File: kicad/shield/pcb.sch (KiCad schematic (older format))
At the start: 10 parts, among them J1 Conn_01x12_Fem_l, J2 Conn_01x12_Fem_r, J3 Conn_01x12_Fem_b_r, J4 Conn_01x09_Fem_b_l

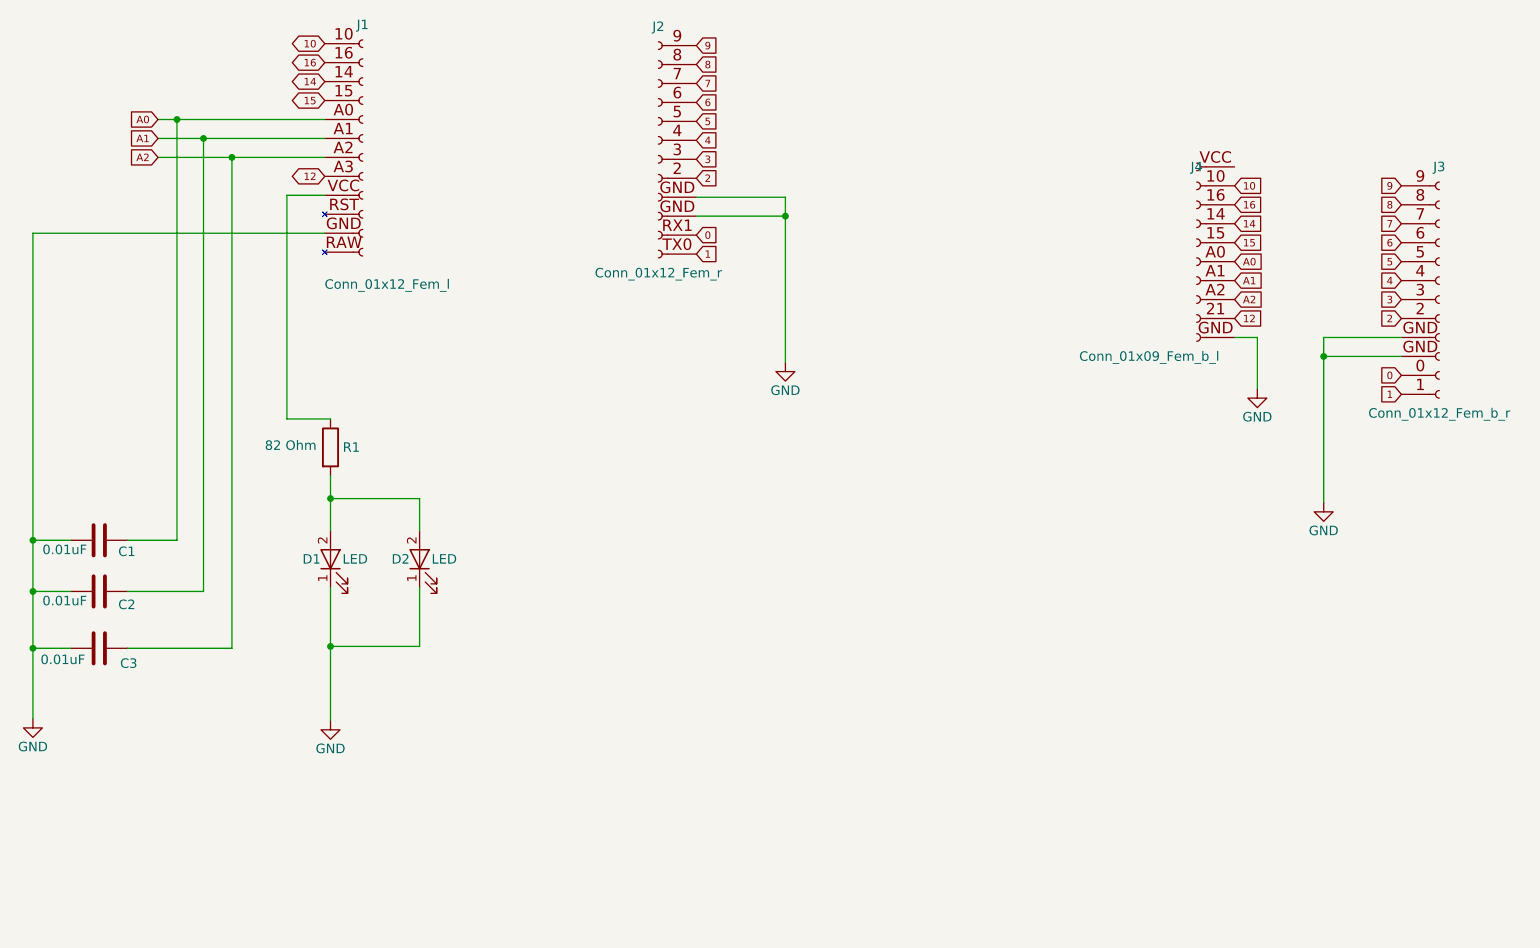
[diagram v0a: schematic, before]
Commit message: update
- verify arduino socket dimension
- change port 12 to 21
- disable TXLED and RXLED
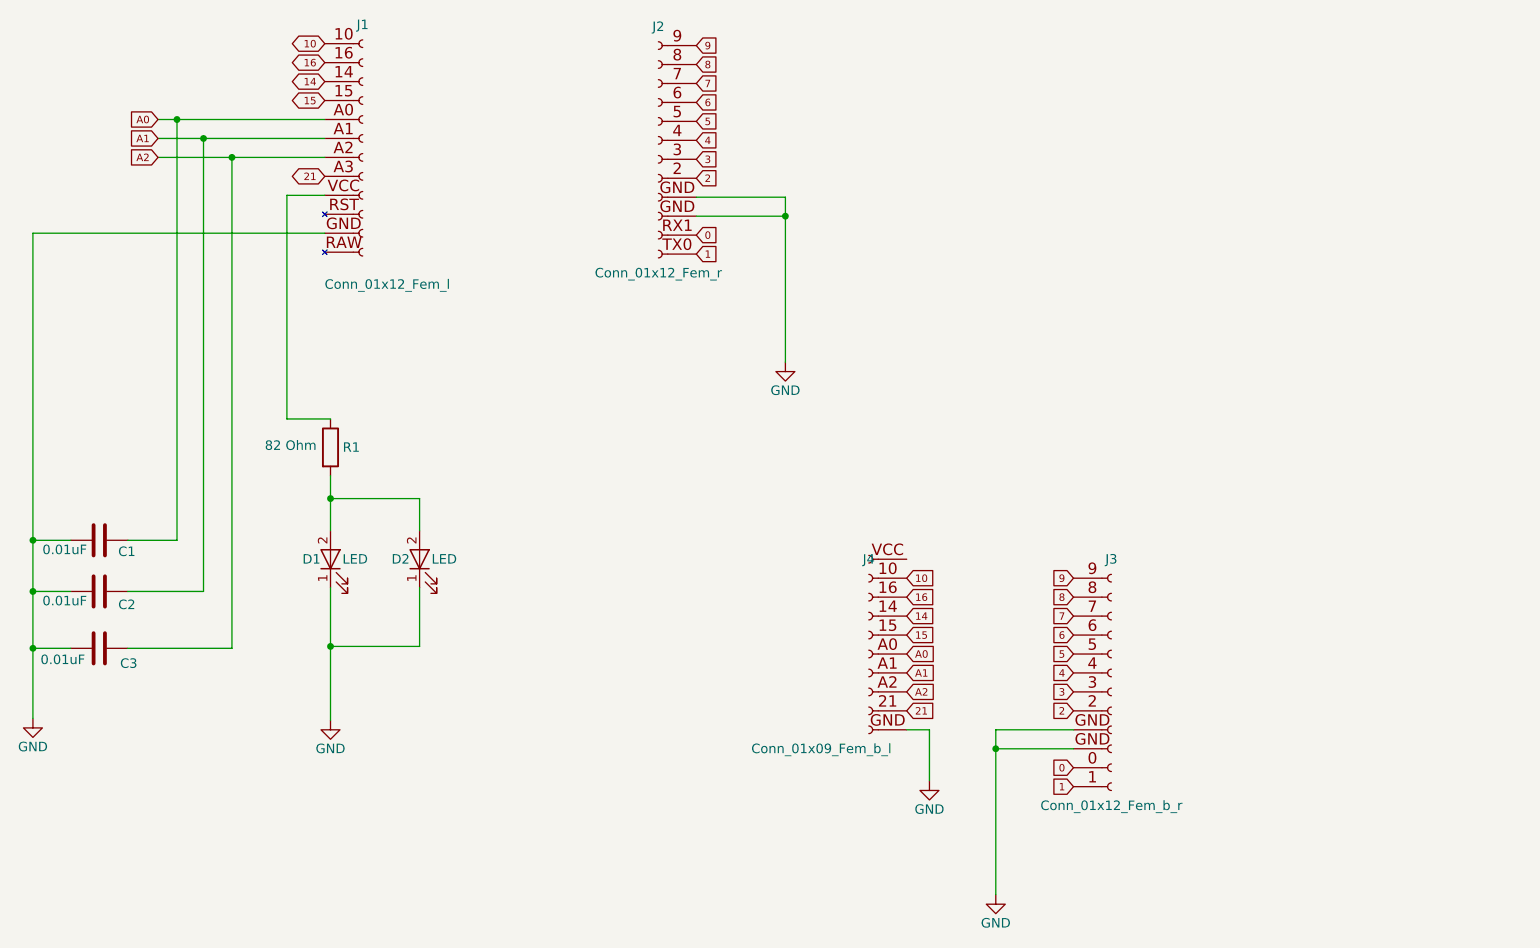
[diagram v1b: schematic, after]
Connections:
- net 12 renamed 21
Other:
- moved on the sheet: J3, J4

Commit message: maybe final
- ultimate PCB design
- add potentiometer for led control
- checked connections
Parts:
- added R2: 2 kOhm, Potentiometers:Potentiometer_Triwood_RM-065, symbol R_Variable
- R1: value 82 Ohm -> 100 Ohm
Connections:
- net at D1.2 (A), D2.2 (A): now also R2.2; no longer R1.2
- new net: R1.2, R2.1
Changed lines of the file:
@@
 	1    0    0    -1
 $EndComp
-$Comp
-L R R1
-U 1 1 5A832FA1
-P 3130 3560
-F 0 "R1" H 3240 3560 50  0000 C CNN
-F 1 "82 Ohm" H 2920 3570 50  0000 C CNN
-F 2 "Resistors_THT:R_Axial_DIN0207_L6.3mm_D2.5mm_P10.16mm_Horizontal" V 3060 3560 50  0001 C CNN
-F 3 "" H 3130 3560 50  0001 C CNN
-	1    3130 3560
-	1    0    0    -1
-$EndComp
 Wire Wire Line
 	3130 3710 3130 4000
@@
 Connection ~ 3130 4610
 Wire Wire Line
-	2900 2230 2900 3410
-Wire Wire Line
 	2900 3410 3130 3410
 $Bitmap
@@
 EndData
 $EndBitmap
+$Comp
+L R_Variable R2
+U 1 1 5A8745C0
+P 3130 3560
+F 0 "R2" H 3270 3510 50  0000 L CNN
+F 1 "2 kOhm" H 3270 3640 50  0000 L CNN
+F 2 "Potentiometers:Potentiometer_Triwood_RM-065" V 3060 3560 50  0001 C CNN
+F 3 "" H 3130 3560 50  0001 C CNN
+	1    3130 3560
+	1    0    0    -1
+$EndComp
+$Comp
+L R R1
+U 1 1 5A879F6C
+P 2900 3090
+F 0 "R1" H 3010 3090 50  0000 C CNN
+F 1 "100 Ohm" H 3140 2980 50  0000 C CNN
+F 2 "Resistors_THT:R_Axial_DIN0207_L6.3mm_D2.5mm_P10.16mm_Horizontal" V 2830 3090 50  0001 C CNN
+F 3 "" H 2900 3090 50  0001 C CNN
+	1    2900 3090
+	1    0    0    -1
+$EndComp
+Wire Wire Line
+	2900 2230 2900 2940
+Wire Wire Line
+	2900 3240 2900 3410
 $EndSCHEMATC

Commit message: VCC pin
- add Vcc pin
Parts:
- J4: footprint Connectors_Samtec:SL-109-X-XX_1x09 -> Connectors_Samtec:SL-110-X-XX_1x10
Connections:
- net VCC: now reaches J1.9 (Pin_9), R1.1
- net VCC: now also J4.1 (Pin_1)
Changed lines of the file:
@@
 U 1 1 5A7C4E7A
 P 5970 4750
-F 0 "J4" H 5970 5350 50  0000 C CNN
+F 0 "J4" H 5840 5540 50  0000 C CNN
 F 1 "Conn_01x09_Fem_b_l" H 6220 4350 50  0000 C CNN
-F 2 "Connectors_Samtec:SL-109-X-XX_1x09" H 5970 4750 50  0001 C CNN
+F 2 "Connectors_Samtec:SL-110-X-XX_1x10" H 5970 4750 50  0001 C CNN
 F 3 "" H 5970 4750 50  0001 C CNN
 	1    5970 4750
@@
 $EndComp
 Wire Wire Line
-	3100 2230 2900 2230
+	2820 2230 3100 2230
 $Comp
 L GND #PWR05
@@
 Wire Wire Line
 	2900 3240 2900 3410
+Text GLabel 2820 2230 0    39   Input ~ 0
+VCC
+Connection ~ 2900 2230
+Text GLabel 6170 4150 2    39   Input ~ 0
+VCC
 $EndSCHEMATC
